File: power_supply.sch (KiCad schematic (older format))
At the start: 68 parts, among them J1 USB-MICRO, J2 USB, Q1 SI4174DY, Q2 SI4463CDY, Q3 SI4463CDY, U1 LM3914, U10 FDC6392S, U11 MCP6041, U2 TPD2E001, U3 MIC2185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

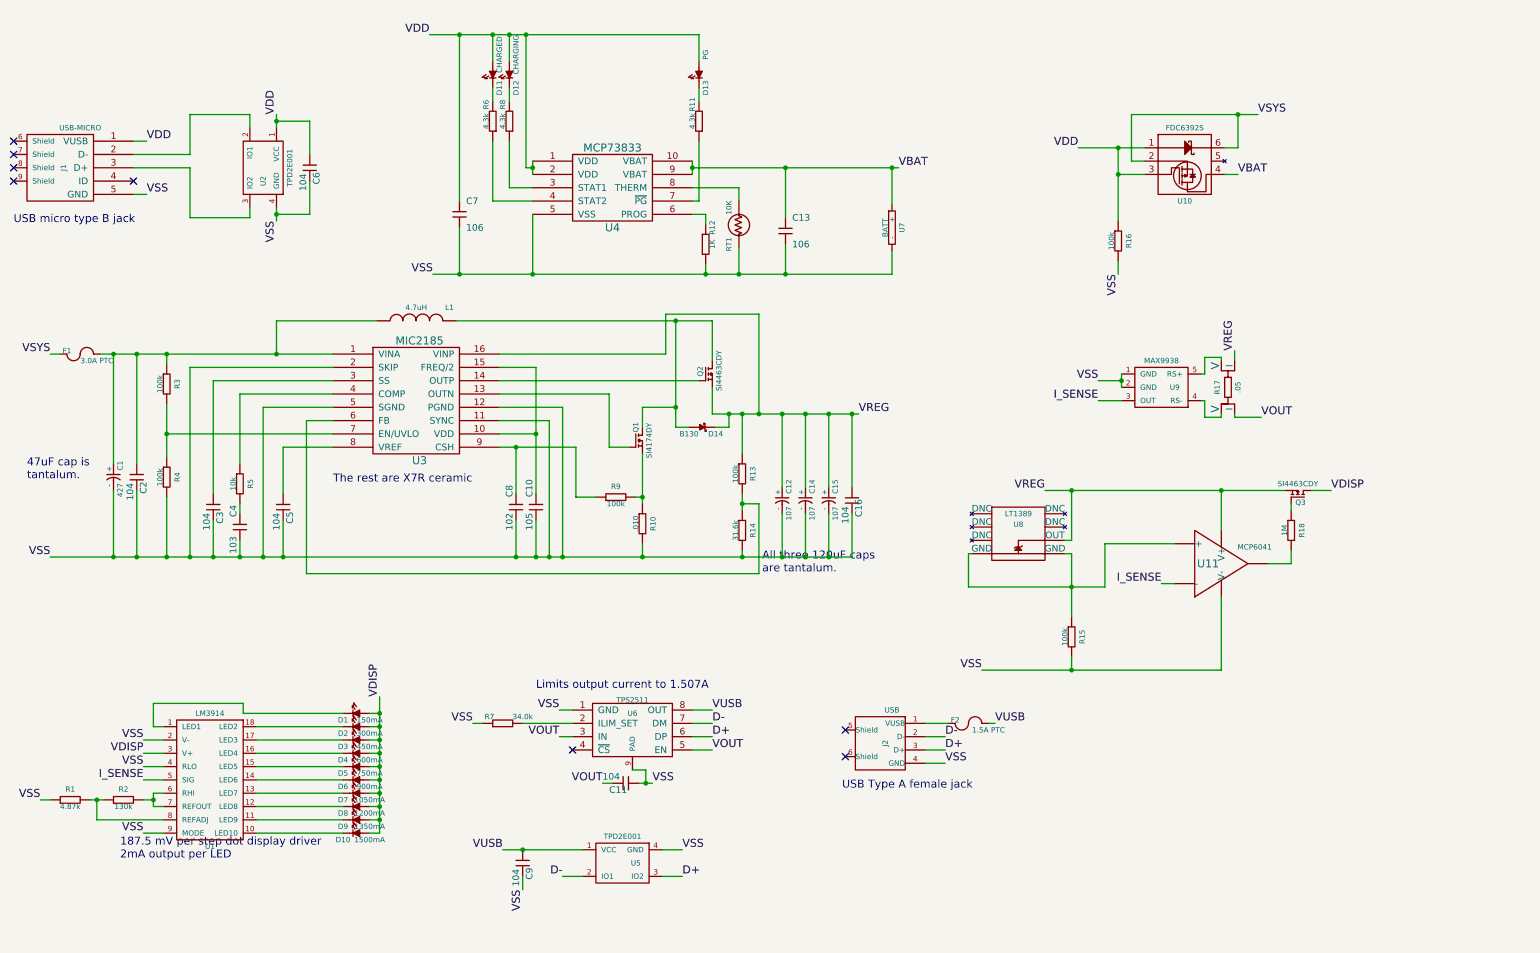
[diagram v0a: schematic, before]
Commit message: Finished rev1 layout
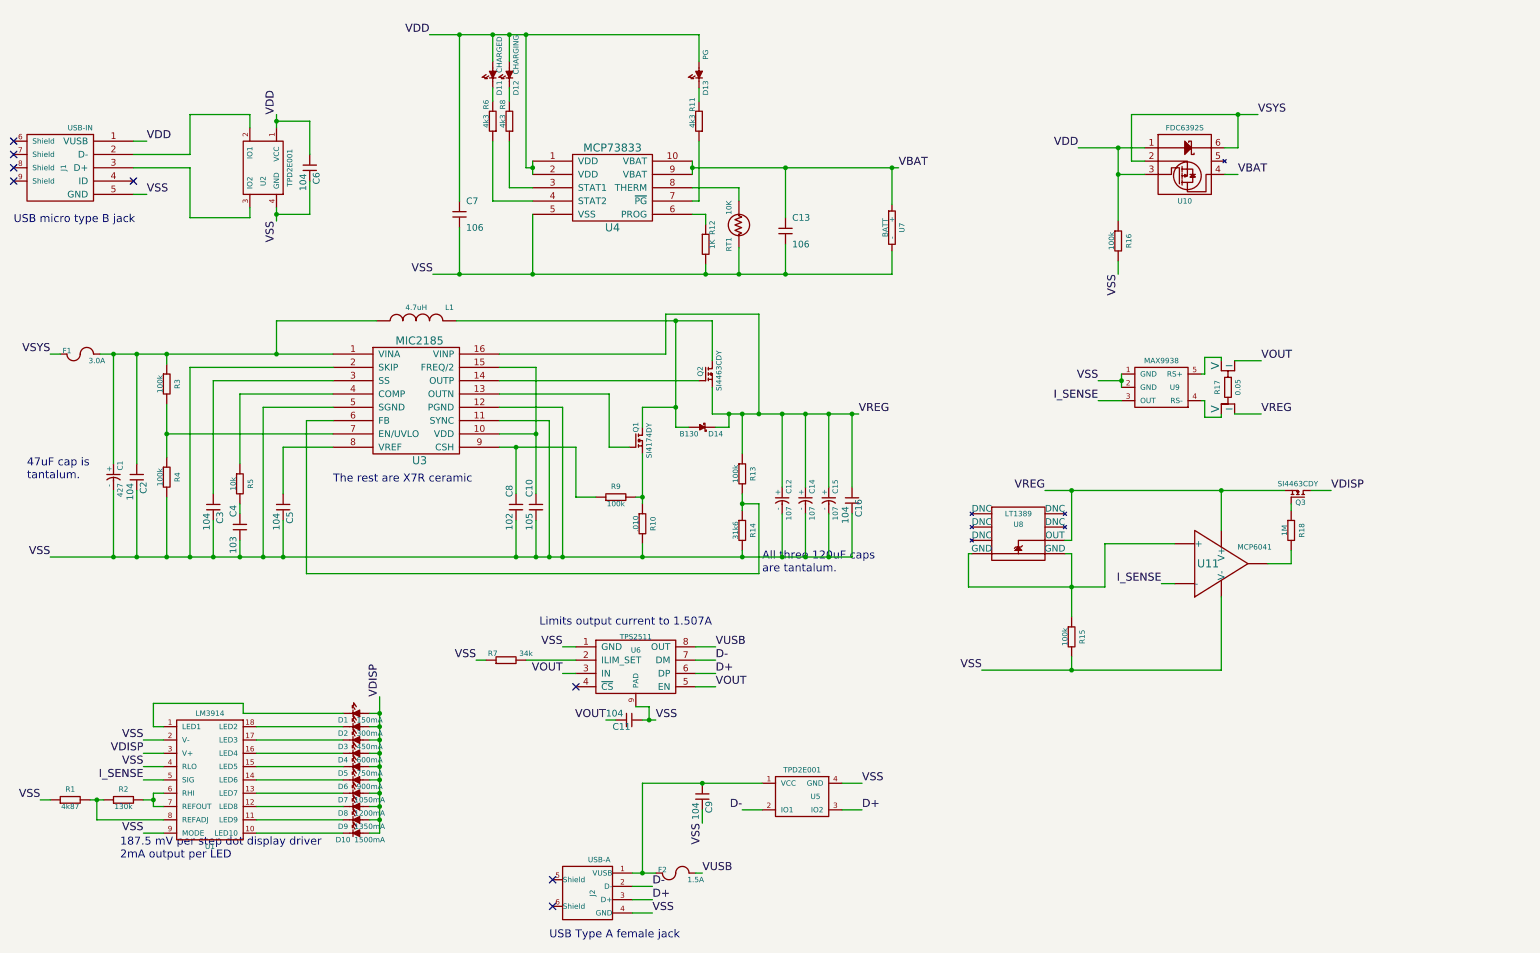
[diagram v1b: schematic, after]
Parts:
- F1: value 3.0A PTC -> 3.0A
- F2: value 1.5A PTC -> 1.5A
- J1: value USB-MICRO -> USB-IN
- J2: value USB -> USB-A
- R1: value 4.87k -> 4k87
- R11, R6, R8: value 4.3k -> 4k3
- R14: value 31.6k -> 31k6
- R17: value .05 -> 0.05
- R7: value 34.0k -> 34k
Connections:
- net VOUT: now also R17.I2 (I); no longer R17.I1 (I)
- net VREG: now also R17.I1 (I); no longer R17.I2 (I)
- net VUSB: no longer C9.1, U5.1 (VCC)
- net at F2.1, J2.1 (VUSB): now also C9.1, U5.1 (VCC)
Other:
- moved on the sheet: C11, C9, F2, J2, R7, U5, U6

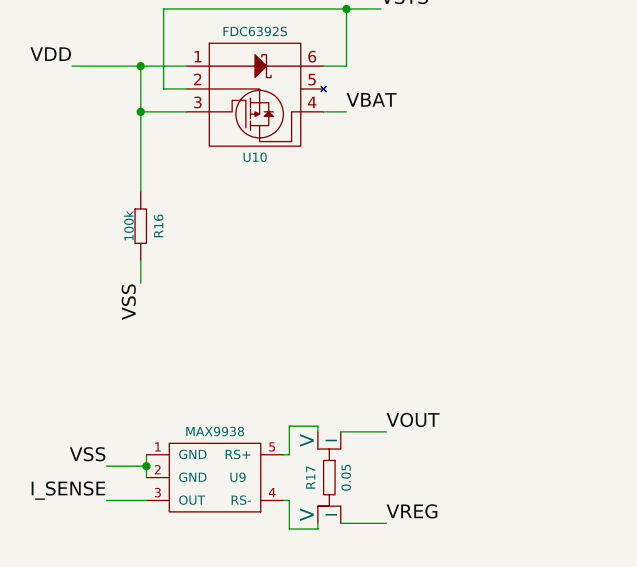
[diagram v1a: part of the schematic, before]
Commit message: Began routing.
Fixed a few footprint issues.
Added through hole vias.
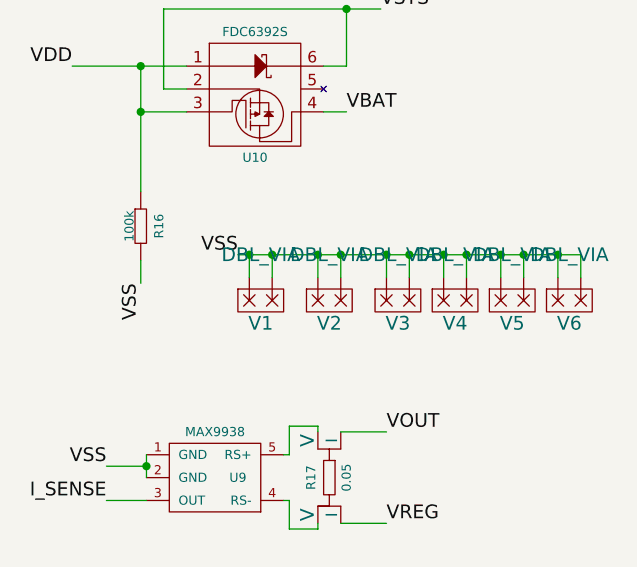
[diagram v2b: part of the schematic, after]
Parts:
- added V1, V2, V3, V4, V5, V6: DBL_VIA, DBL_VIA, symbol DBL_VIA
- C1: footprint ~ -> c_2917_tant
- C10, C4, C8: footprint (none) -> cp_2.54mm
- C11, C13, C16, C2, C3, C5, C6, C7, C9: footprint (none) -> c_1206
- C12, C14, C15: footprint ~ -> c_2924_tant
- D1, D10, D11, D12, D13, D2, D3, D4, D5, D6, D7, D8, D9: footprint ~ -> led_1206
- D14: footprint (none) -> diode_do41
- F1, F2: footprint (none) -> ptc_1812
- J1: footprint (none) -> A108263CT(uUSB)
- J2: footprint ~ -> A107360(USB-A)
- L1: footprint ~ -> ind_12.5mm
- Q1: footprint ~ -> si4174dy
- Q2, Q3: footprint ~ -> si4463cdy
- R1, R11, R18, R2, R5, R6, R7, R8: footprint ~ -> r_pth_2.5x6.5mm
- R10, R13, R14, R15, R16, R3, R4, R9: footprint ~ -> r_1206
- R12, RT1: footprint (none) -> r_1206
- R17: footprint ~ -> 1206-Kelvin
- U1: footprint (none) -> PDIP-18
- U10: footprint (none) -> sot23-6
- U11: footprint ~ -> so-8
- U2, U5: footprint ~ -> TO-253-4
- U3: footprint (none) -> so-16
- U4: footprint ~ -> msop-10
- U6: footprint (none) -> msop-8-powerpad
- U7: footprint (none) -> BAT-18650-cylinder
- U8: footprint (none) -> so-8
- U9: footprint (none) -> sot23-5
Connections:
- net VSS: now also V1.1, V1.2, V2.1, V2.2, V3.1, V3.2, V4.1, V4.2, V5.1, V5.2, V6.1, V6.2

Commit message: More routing work
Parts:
- added V10, V7, V8, V9: DBL_VIA, DBL_VIA, symbol DBL_VIA
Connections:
- net VSS: now also V10.1, V10.2, V7.1, V7.2, V8.1, V8.2, V9.1, V9.2
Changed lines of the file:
@@
 Sheet 1 1
 Title "USB Power Pack"
-Date "21 jun 2014"
+Date "22 jun 2014"
 Rev "2"
 Comp "AMP Lab"
@@
 	9550 2600 9550 2500
 Wire Wire Line
-	9500 2500 11000 2500
+	9500 2500 12000 2500
 Wire Wire Line
 	11000 2500 11000 2600
@@
 VSS
 Connection ~ 9550 2500
+$Comp
+L DBL_VIA V7
+U 1 1 53A65E51
+P 11200 2650
+F 0 "V7" H 11200 2500 60  0000 C CNN
+F 1 "DBL_VIA" H 11200 2800 60  0000 C CNN
+F 2 "DBL_VIA" H 11200 2650 60  0001 C CNN
+F 3 "" H 11200 2650 60  0000 C CNN
+	1    11200 2650
+	1    0    0    -1
+$EndComp
+$Comp
+L DBL_VIA V8
+U 1 1 53A65E57
+P 11450 2650
+F 0 "V8" H 11450 2500 60  0000 C CNN
+F 1 "DBL_VIA" H 11450 2800 60  0000 C CNN
+F 2 "DBL_VIA" H 11450 2650 60  0001 C CNN
+F 3 "" H 11450 2650 60  0000 C CNN
+	1    11450 2650
+	1    0    0    -1
+$EndComp
+$Comp
+L DBL_VIA V9
+U 1 1 53A65E5D
+P 11700 2650
+F 0 "V9" H 11700 2500 60  0000 C CNN
+F 1 "DBL_VIA" H 11700 2800 60  0000 C CNN
+F 2 "DBL_VIA" H 11700 2650 60  0001 C CNN
+F 3 "" H 11700 2650 60  0000 C CNN
+	1    11700 2650
+	1    0    0    -1
+$EndComp
+$Comp
+L DBL_VIA V10
+U 1 1 53A65E63
+P 11950 2650
+F 0 "V10" H 11950 2500 60  0000 C CNN
+F 1 "DBL_VIA" H 11950 2800 60  0000 C CNN
+F 2 "DBL_VIA" H 11950 2650 60  0001 C CNN
+F 3 "" H 11950 2650 60  0000 C CNN
+	1    11950 2650
+	1    0    0    -1
+$EndComp
+Wire Wire Line
+	12000 2500 12000 2600
+Wire Wire Line
+	11900 2600 11900 2500
+Wire Wire Line
+	11750 2600 11750 2500
+Wire Wire Line
+	11650 2600 11650 2500
+Wire Wire Line
+	11500 2600 11500 2500
+Wire Wire Line
+	11400 2600 11400 2500
+Connection ~ 11000 2500
+Wire Wire Line
+	11150 2600 11150 2500
+Connection ~ 11150 2500
+Wire Wire Line
+	11250 2600 11250 2500
+Connection ~ 11250 2500
+Connection ~ 11400 2500
+Connection ~ 11500 2500
+Connection ~ 11650 2500
+Connection ~ 11750 2500
+Connection ~ 11900 2500
 $EndSCHEMATC

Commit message: Finished routing
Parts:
- added R19: 100k, r_1206, symbol R
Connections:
- net I_SENSE: now also R19.2; no longer U11.2 (-)
- new net: R19.1, U11.2 (-)
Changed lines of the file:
@@
 	1    0    0    -1
 $EndComp
-Text Label 9400 4950 2    60   ~ 0
+Text Label 9100 4950 3    60   ~ 0
 I_SENSE
 $Comp
@@
 	8725 5600 8725 5500
 Wire Wire Line
-	9400 4950 9500 4950
-Wire Wire Line
 	7950 4975 8975 4975
 Wire Wire Line
@@
 Wire Wire Line
 	8050 5600 9850 5600
-Wire Wire Line
-	8975 4650 9500 4650
 Wire Wire Line
 	8975 4975 8975 4650
@@
 Connection ~ 11750 2500
 Connection ~ 11900 2500
+$Comp
+L R R19
+U 1 1 53A70602
+P 9300 4950
+F 0 "R19" V 9380 4950 40  0000 C CNN
+F 1 "100k" V 9250 4950 40  0000 C CNN
+F 2 "r_1206" V 9230 4950 30  0001 C CNN
+F 3 "http://www.vishay.com/doc?20035" H 9300 4950 30  0001 C CNN
+F 4 "541-100KFCT-ND" V 9300 4950 60  0001 C CNN "Product Number"
+F 5 "Digikey" V 9300 4950 60  0001 C CNN "Vendor"
+	1    9300 4950
+	0    1    1    0
+$EndComp
+Wire Wire Line
+	8975 4650 9500 4650
+Wire Wire Line
+	9100 4950 9150 4950
+Wire Wire Line
+	9450 4950 9500 4950
 $EndSCHEMATC

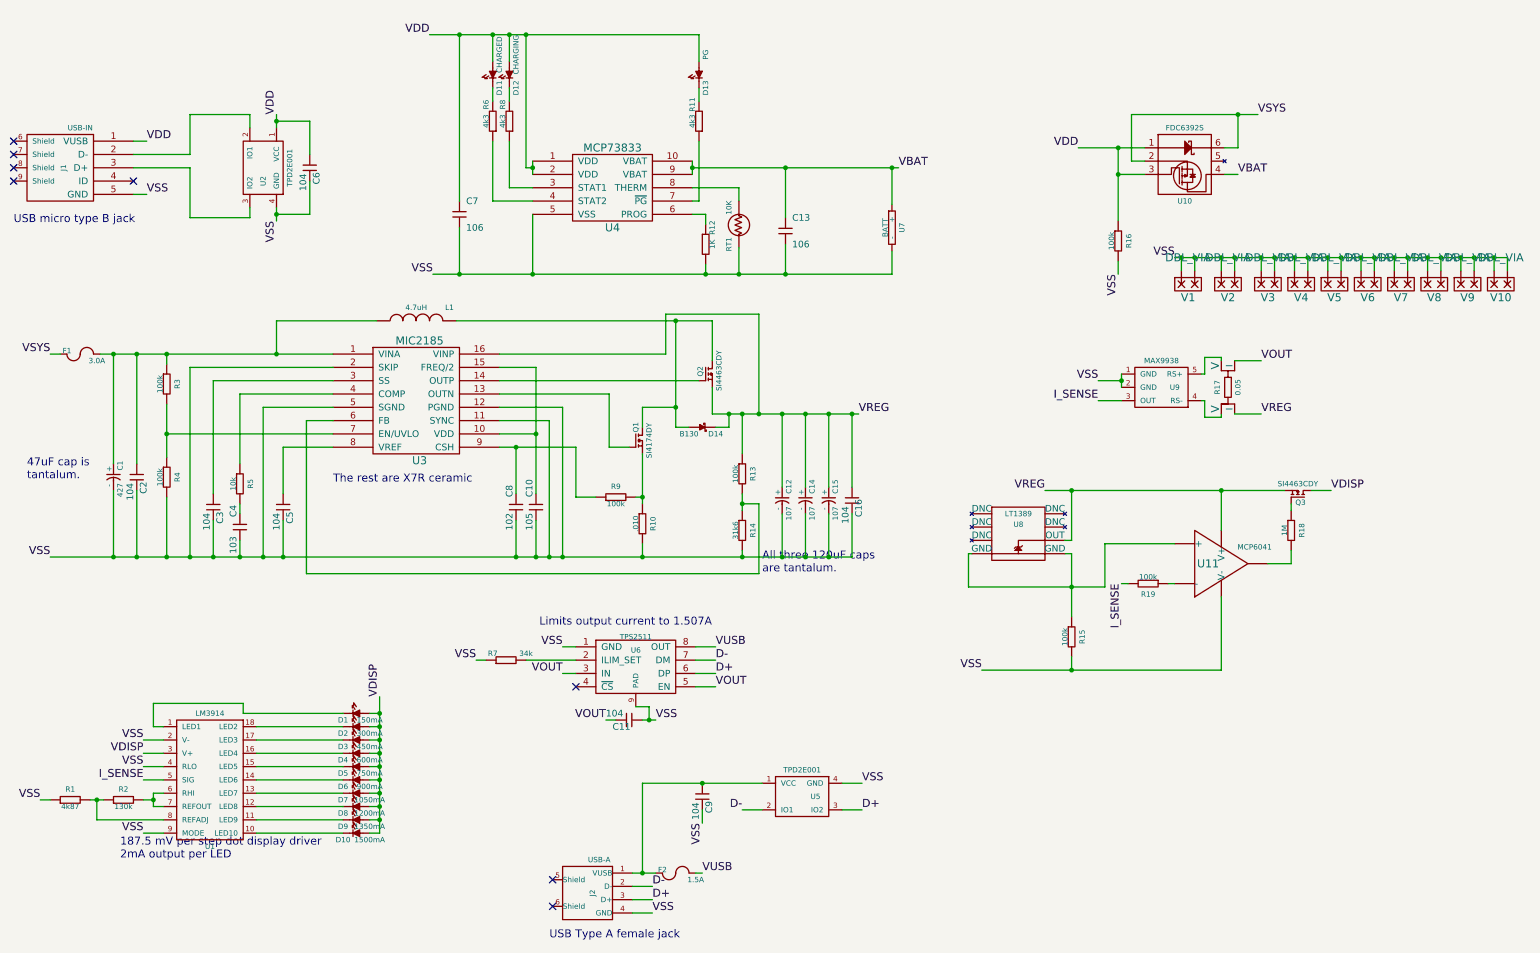
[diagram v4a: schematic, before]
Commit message: Fixed issues in response to Bob's comments
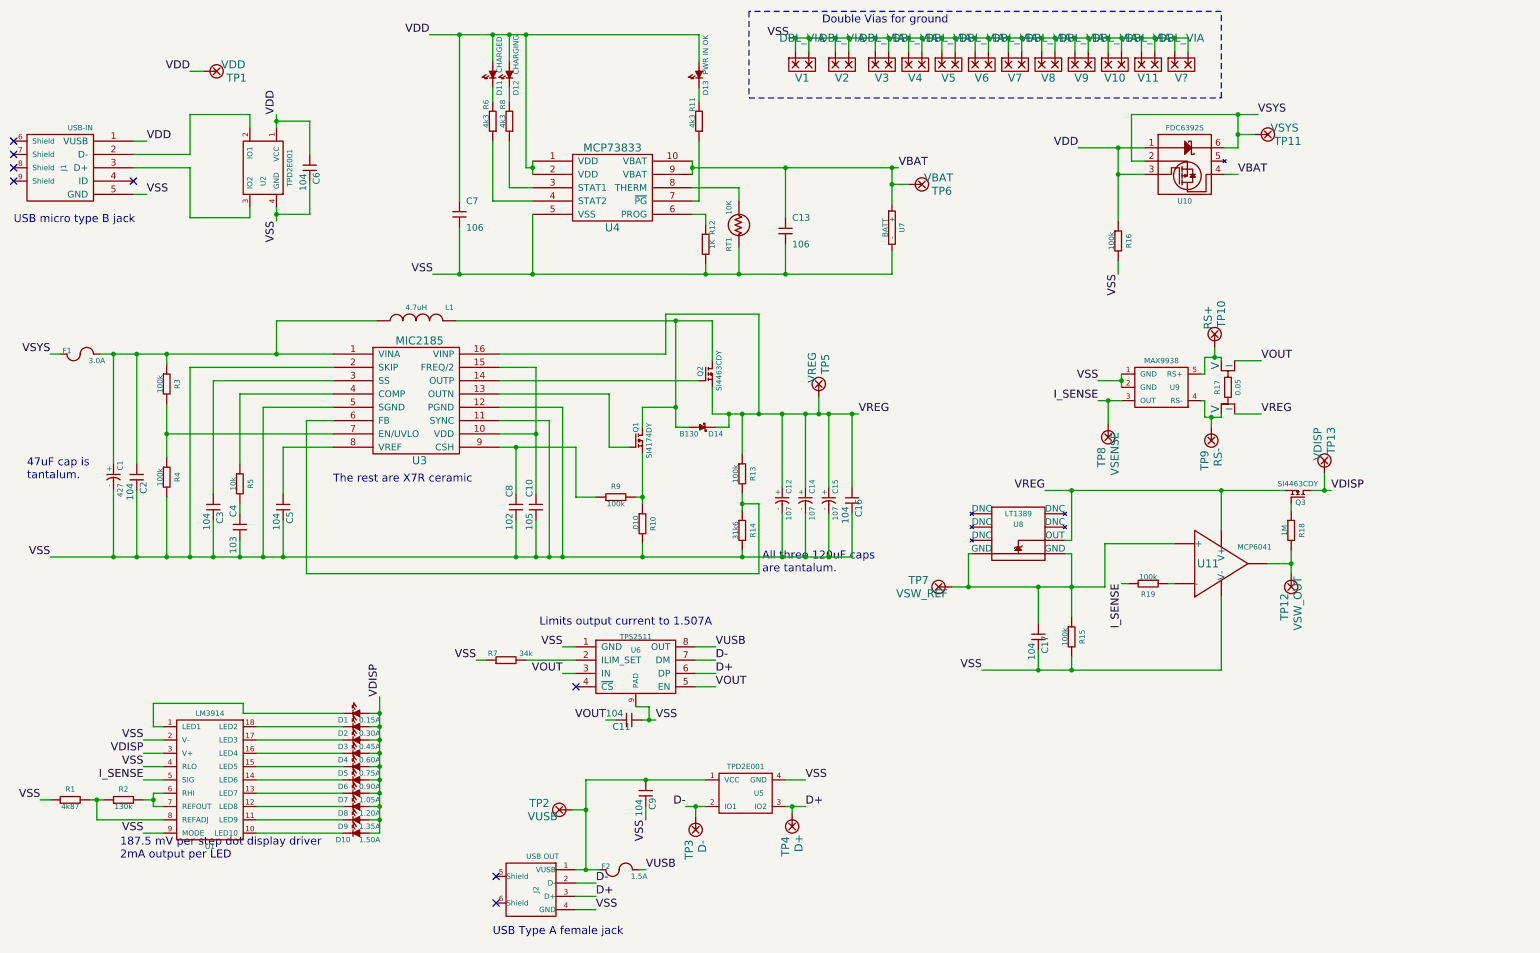
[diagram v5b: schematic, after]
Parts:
- added C17: 104, c_1206, symbol C
- added TP1: VDD, symbol TP
- added TP10: RS+, symbol TP
- added TP11: VSYS, symbol TP
- added TP12: VSW_OUT, symbol TP
- added TP13: VDISP, symbol TP
- added TP2: VUSB, symbol TP
- added TP3: D-, symbol TP
- added TP4: D+, symbol TP
- added TP5: VREG, symbol TP
- added TP6: VBAT, symbol TP
- added TP7: VSW_REF, symbol TP
- added TP8: VSENSE, symbol TP
- added TP9: RS-, symbol TP
- added V11, V?: DBL_VIA, DBL_VIA, symbol DBL_VIA
- D1: value 150mA -> 0.15A
- D10: value 1500mA -> 1.50A
- D13: value PG -> PWR IN OK
- D2: value 300mA -> 0.30A
- D3: value 450mA -> 0.45A
- D4: value 600mA -> 0.60A
- D5: value 750mA -> 0.75A
- D6: value 900mA -> 0.90A
- D7: value 1050mA -> 1.05A
- D8: value 1200mA -> 1.20A
- D9: value 1350mA -> 1.35A
- J2: value USB-A -> USB OUT
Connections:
- net D+: now also TP4.1
- net D-: now also TP3.1
- net I_SENSE: now also TP8.1
- net VBAT: now also TP6.1
- net VDD: now also TP1.1
- net VDISP: now also TP13.1
- net VREG: now also TP5.1
- net VSS: now also C17.2, V11.1, V11.2, V?.1, V?.2
- net VSYS: now also TP11.1
- net at R17.V1 (V), U9.4 (RS-): now also TP9.1
- net at R17.V2 (V), U9.5 (RS+): now also TP10.1
- net at C9.1, F2.1, J2.1 (VUSB)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: now also TP2.1
- net at R18.2, U11.6: now also TP12.1
- net at R15.1, U11.3 (+), U8.4 (GND)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: now also C17.1, TP7.1
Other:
- note added: "Double Vias for ground"
- moved on the sheet: C9, F2, J2, U5, V1, V10, V2, V3, V4, V5, V6, V7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

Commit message: More fixes
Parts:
- gave numbers to parts that had none: 1
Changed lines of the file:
@@
 Connection ~ 8475 5600
 $Comp
-L DBL_VIA V?
+L DBL_VIA V12
 U 1 1 53A9D07E
 P 9550 1000
-F 0 "V?" H 9550 850 60  0000 C CNN
+F 0 "V12" H 9550 850 60  0000 C CNN
 F 1 "DBL_VIA" H 9550 1150 60  0000 C CNN
 F 2 "DBL_VIA" H 9550 1000 60  0001 C CNN
